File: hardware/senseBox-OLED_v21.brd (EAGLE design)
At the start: 45 x 25 mm, 28 parts, among them IC2 VREG-TS9011-3V3, IC4 MAX8XX-809R, J1 JUMPER2-0402-NC, J2 JST4-B4B-PH-SM4-TB, T3 BSS138PS, X1 PASSER-07, X2 PASSER-07, X3 PASSER-07, X4 PASSER-07

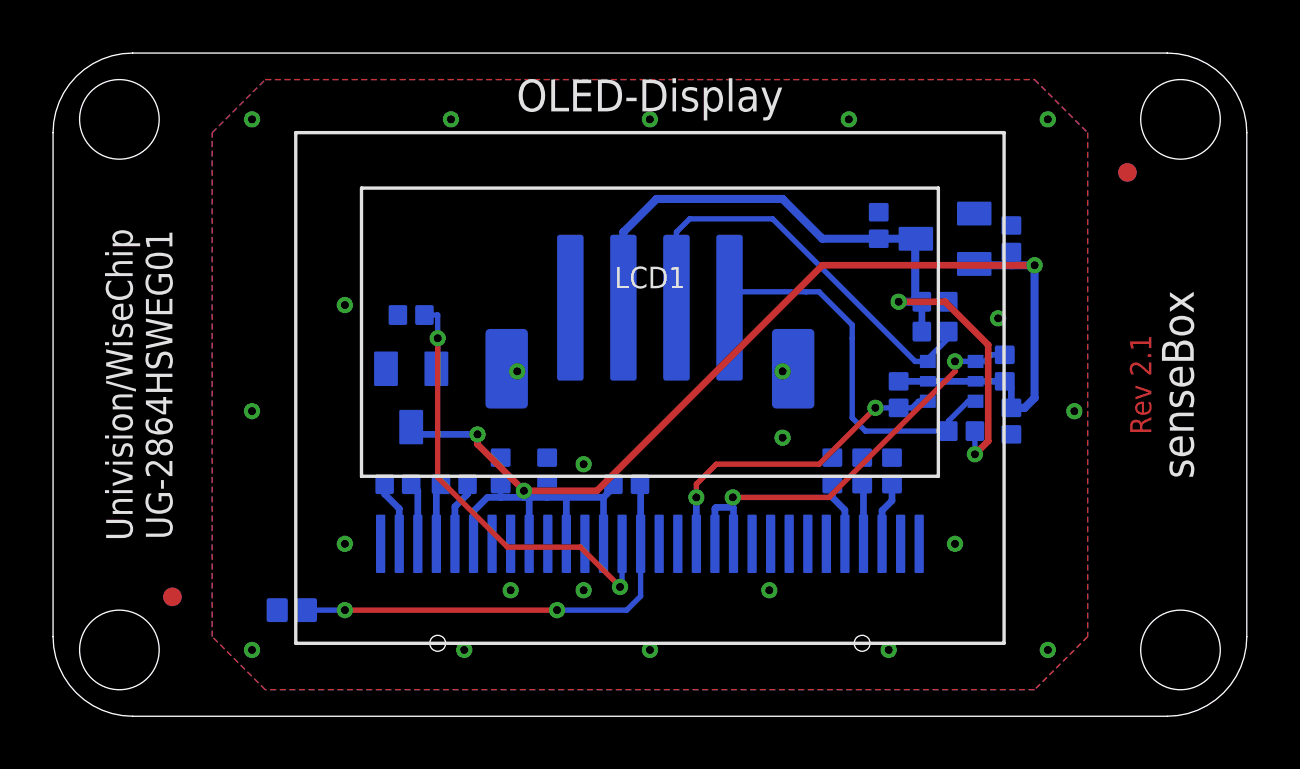
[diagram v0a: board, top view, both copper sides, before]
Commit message: updated schematics
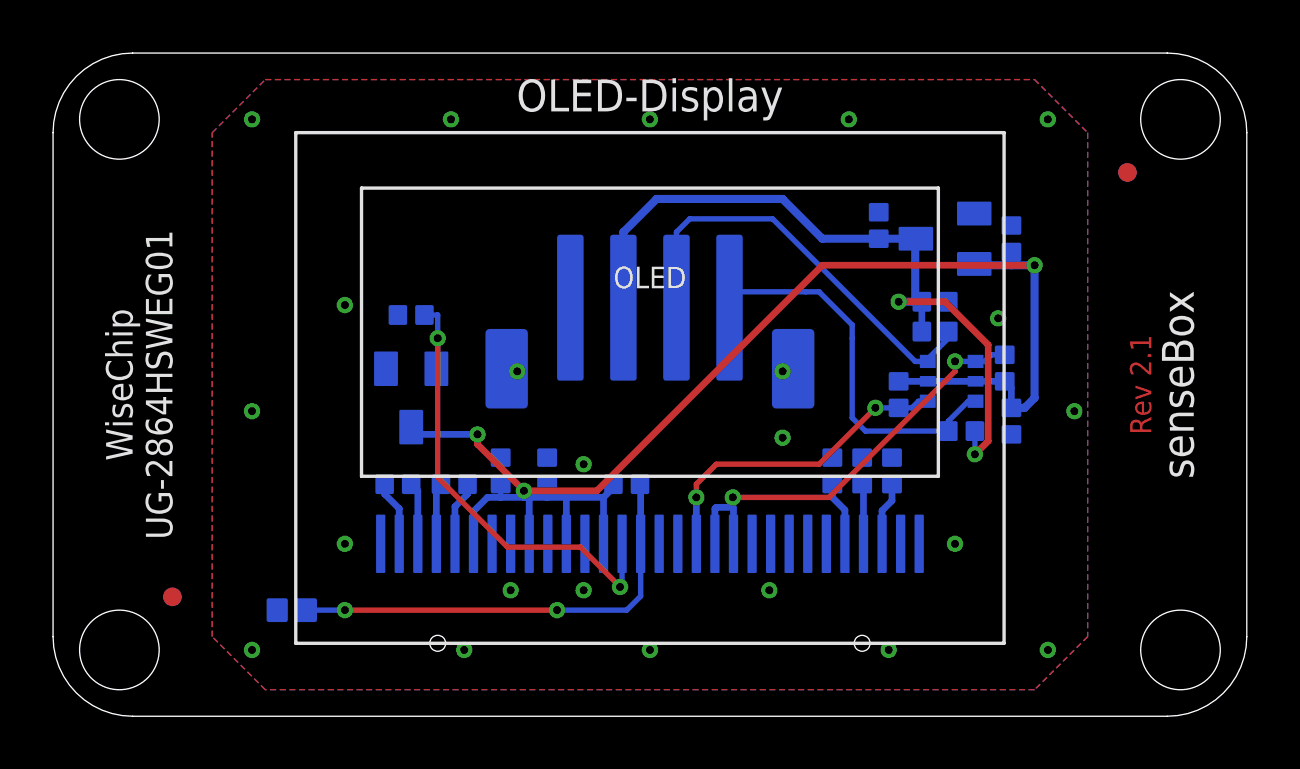
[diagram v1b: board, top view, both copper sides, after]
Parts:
- renumbered LCD1 to OLED
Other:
- board text added: "WiseChip UG-2864HSWEG01"
- board text removed: "Univision/WiseChip UG-2864HSWEG01"
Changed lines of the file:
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@@
 <text x="8.125" y="6.25" size="0.8" layer="22" font="vector" ratio="15" rot="MR90">0x3C closed</text>
 <text x="9.25" y="6.25" size="0.8" layer="22" font="vector" ratio="15" rot="MR90">0x3D open</text>
-<text x="2" y="12.5" size="1" layer="21" font="vector" ratio="15" rot="R90" align="top-center">Univision/WiseChip
+<text x="2" y="12.5" size="1" layer="21" font="vector" ratio="15" rot="R90" align="top-center">WiseChip
 UG-2864HSWEG01</text>
 <wire x1="10.25" y1="4.75" x2="7.75" y2="4.75" width="0.2" layer="22"/>
@@
 <element name="C4" library="we-rcl" package="C0402" value="100n" x="36.125" y="11.125" rot="MR180"/>
 <element name="C1" library="we-rcl" package="C0402" value="100n" x="33.25" y="15.625" rot="MR90"/>
-<element name="LCD1" library="we-opto" package="UG2864HSWEG01_BOT" value="UG2864HSWEG01-B" x="22.5" y="2.75"/>
+<element name="OLED" library="we-opto" package="UG2864HSWEG01_BOT" value="UG2864HSWEG01-B" x="22.5" y="2.75"/>
 <element name="R6" library="we-rcl" package="C0402" value="4k7" x="21.625" y="8.75" rot="MR90"/>
 <element name="C6" library="we-rcl" package="C0402" value="2u2" x="31.625" y="9.25" rot="MR0"/>
@@
 <contactref element="C4" pad="1"/>
 <contactref element="C1" pad="1"/>
-<contactref element="LCD1" pad="12"/>
+<contactref element="OLED" pad="12"/>
 <contactref element="J1" pad="1"/>
-<contactref element="LCD1" pad="29"/>
-<contactref element="LCD1" pad="30"/>
-<contactref element="LCD1" pad="1"/>
-<contactref element="LCD1" pad="8"/>
+<contactref element="OLED" pad="29"/>
+<contactref element="OLED" pad="30"/>
+<contactref element="OLED" pad="1"/>
+<contactref element="OLED" pad="8"/>
 <contactref element="R5" pad="2"/>
 <contactref element="C5" pad="1"/>
@@
 <contactref element="C7" pad="1"/>
 <contactref element="C6" pad="1"/>
-<contactref element="LCD1" pad="10"/>
+<contactref element="OLED" pad="10"/>
 <via x="7.5" y="22.5" extent="1-16" drill="0.3"/>
 <contactref element="J2" pad="1"/>
@@
 <contactref element="IC2" pad="2"/>
 <contactref element="C4" pad="2"/>
-<contactref element="LCD1" pad="13"/>
-<contactref element="LCD1" pad="11"/>
+<contactref element="OLED" pad="13"/>
+<contactref element="OLED" pad="11"/>
 <contactref element="R6" pad="2"/>
-<contactref element="LCD1" pad="6"/>
+<contactref element="OLED" pad="6"/>
 <contactref element="C8" pad="2"/>
-<contactref element="LCD1" pad="9"/>
+<contactref element="OLED" pad="9"/>
 <contactref element="C7" pad="2"/>
 <wire x1="15.85" y1="6.5" x2="15.85" y2="7.725" width="0.254" layer="16"/>
@@
 <contactref element="R1" pad="1"/>
 <contactref element="T3" pad="1"/>
-<contactref element="LCD1" pad="20"/>
-<contactref element="LCD1" pad="19"/>
+<contactref element="OLED" pad="20"/>
+<contactref element="OLED" pad="19"/>
 <wire x1="25.65" y1="6.5" x2="25.65" y2="7.85" width="0.254" layer="16"/>
 <wire x1="25.65" y1="7.85" x2="25.625" y2="7.875" width="0.2032" layer="16"/>
@@
 <contactref element="R4" pad="1"/>
 <contactref element="T3" pad="4"/>
-<contactref element="LCD1" pad="18"/>
+<contactref element="OLED" pad="18"/>
 <wire x1="32.975" y1="11.875" x2="32.625" y2="11.875" width="0.2032" layer="16"/>
 <wire x1="32.625" y1="11.875" x2="32.375" y2="11.625" width="0.2032" layer="16"/>
@@
 </signal>
 <signal name="SA0">
-<contactref element="LCD1" pad="15"/>
+<contactref element="OLED" pad="15"/>
 <contactref element="R6" pad="1"/>
 <contactref element="J1" pad="2"/>
@@
 </signal>
 <signal name="C2N">
-<contactref element="LCD1" pad="3"/>
+<contactref element="OLED" pad="3"/>
 <contactref element="C9" pad="1"/>
 <wire x1="13.75" y1="6.5" x2="13.75" y2="8.5" width="0.254" layer="16"/>
@@
 </signal>
 <signal name="C2P">
-<contactref element="LCD1" pad="2"/>
+<contactref element="OLED" pad="2"/>
 <contactref element="C9" pad="2"/>
 <wire x1="13.05" y1="6.5" x2="13.05" y2="7.825" width="0.254" layer="16"/>
@@
 </signal>
 <signal name="C1N">
-<contactref element="LCD1" pad="5"/>
+<contactref element="OLED" pad="5"/>
 <contactref element="C10" pad="1"/>
 <wire x1="15.15" y1="6.5" x2="15.15" y2="7.9" width="0.254" layer="16"/>
@@
 </signal>
 <signal name="C1P">
-<contactref element="LCD1" pad="4"/>
+<contactref element="OLED" pad="4"/>
 <contactref element="C10" pad="2"/>
 <wire x1="14.45" y1="6.5" x2="14.45" y2="8.575" width="0.254" layer="16"/>
@@
 </signal>
 <signal name="IREF">
-<contactref element="LCD1" pad="26"/>
+<contactref element="OLED" pad="26"/>
 <contactref element="R5" pad="1"/>
 <wire x1="29.85" y1="6.5" x2="29.85" y2="7.775" width="0.254" layer="16"/>
@@
 </signal>
 <signal name="VCH">
-<contactref element="LCD1" pad="27"/>
+<contactref element="OLED" pad="27"/>
 <contactref element="C5" pad="2"/>
 <wire x1="30.55" y1="6.5" x2="30.55" y2="8.7" width="0.254" layer="16"/>
@@
 </signal>
 <signal name="VC">
-<contactref element="LCD1" pad="28"/>
+<contactref element="OLED" pad="28"/>
 <contactref element="C6" pad="2"/>
 <wire x1="31.25" y1="6.5" x2="31.25" y2="7.75" width="0.254" layer="16"/>
@@
 </signal>
 <signal name="RST">
-<contactref element="LCD1" pad="14"/>
+<contactref element="OLED" pad="14"/>
 <contactref element="IC4" pad="2"/>
 <wire x1="21.45" y1="6.5" x2="21.45" y2="4.95" width="0.2032" layer="16"/>
